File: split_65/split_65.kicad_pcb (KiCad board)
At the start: 2 copper layers, 156 parts, among them SW1 SW_Push, SW10 SW_Push, SW11 SW_Push, SW12 SW_Push, SW13 SW_Push, SW14 SW_Push, SW15 SW_Push, SW16 SW_Push, SW17 SW_Push, SW18 SW_Push, SW19 SW_Push, SW2 SW_Push, SW20 SW_Push, SW21 SW_Push, SW22 SW_Push, SW23 SW_Push, SW24 SW_Push, SW25 SW_Push, SW26 SW_Push, SW27 SW_Push, SW28 SW_Push, SW29 SW_Push, SW3 SW_Push, SW30 SW_Push, SW31 SW_Push, SW32 SW_Push, SW33 SW_Push, SW34 SW_Push, SW35 SW_Push, SW36 SW_Push, SW37 SW_Push, SW38 SW_Push, SW39 SW_Push, SW4 SW_Push, SW40 SW_Push, SW41 SW_Push, SW42 SW_Push, SW43 SW_Push, SW44 SW_Push, SW45 SW_Push, SW46 SW_Push, SW47 SW_Push, SW48 SW_Push, SW49 SW_Push, SW5 SW_Push, SW50 SW_Push, SW51 SW_Push, SW52 SW_Push, SW53 SW_Push, SW54 SW_Push, SW55 SW_Push, SW56 SW_Push, SW57 SW_Push, SW58 SW_Push, SW59 SW_Push, SW6 SW_Push, SW60 SW_Push, SW61 SW_Push, SW62 SW_Push, SW63 SW_Push, SW64 SW_Push, SW65 SW_Push, SW66 SW_Push, SW67 SW_Push, SW68 SW_Push, SW69 SW_Push, SW7 SW_Push, SW70 SW_Push, SW71 SW_Push, SW72 SW_Push, SW73 SW_Push, SW74 SW_Push, SW75 SW_Push, SW76 SW_Push, SW77 SW_Push, SW78 SW_Push, SW79 SW_Push, SW8 SW_Push, SW80 SW_Push, SW81 SW_Push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

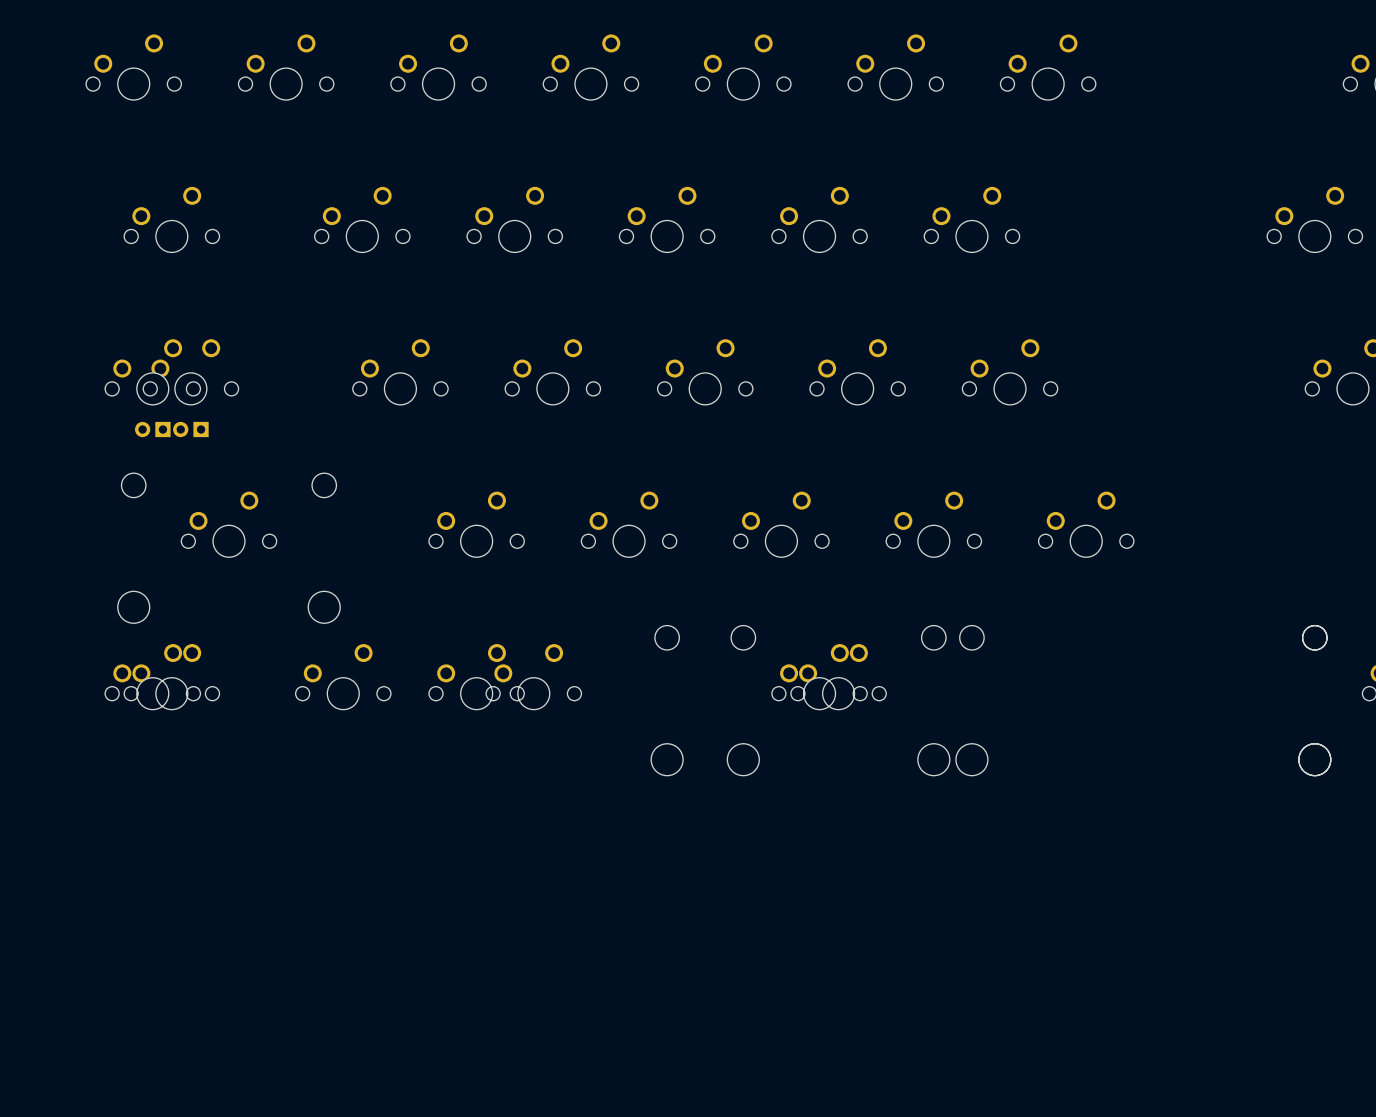
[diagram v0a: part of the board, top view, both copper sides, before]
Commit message: setup schematic hierarchies, update images
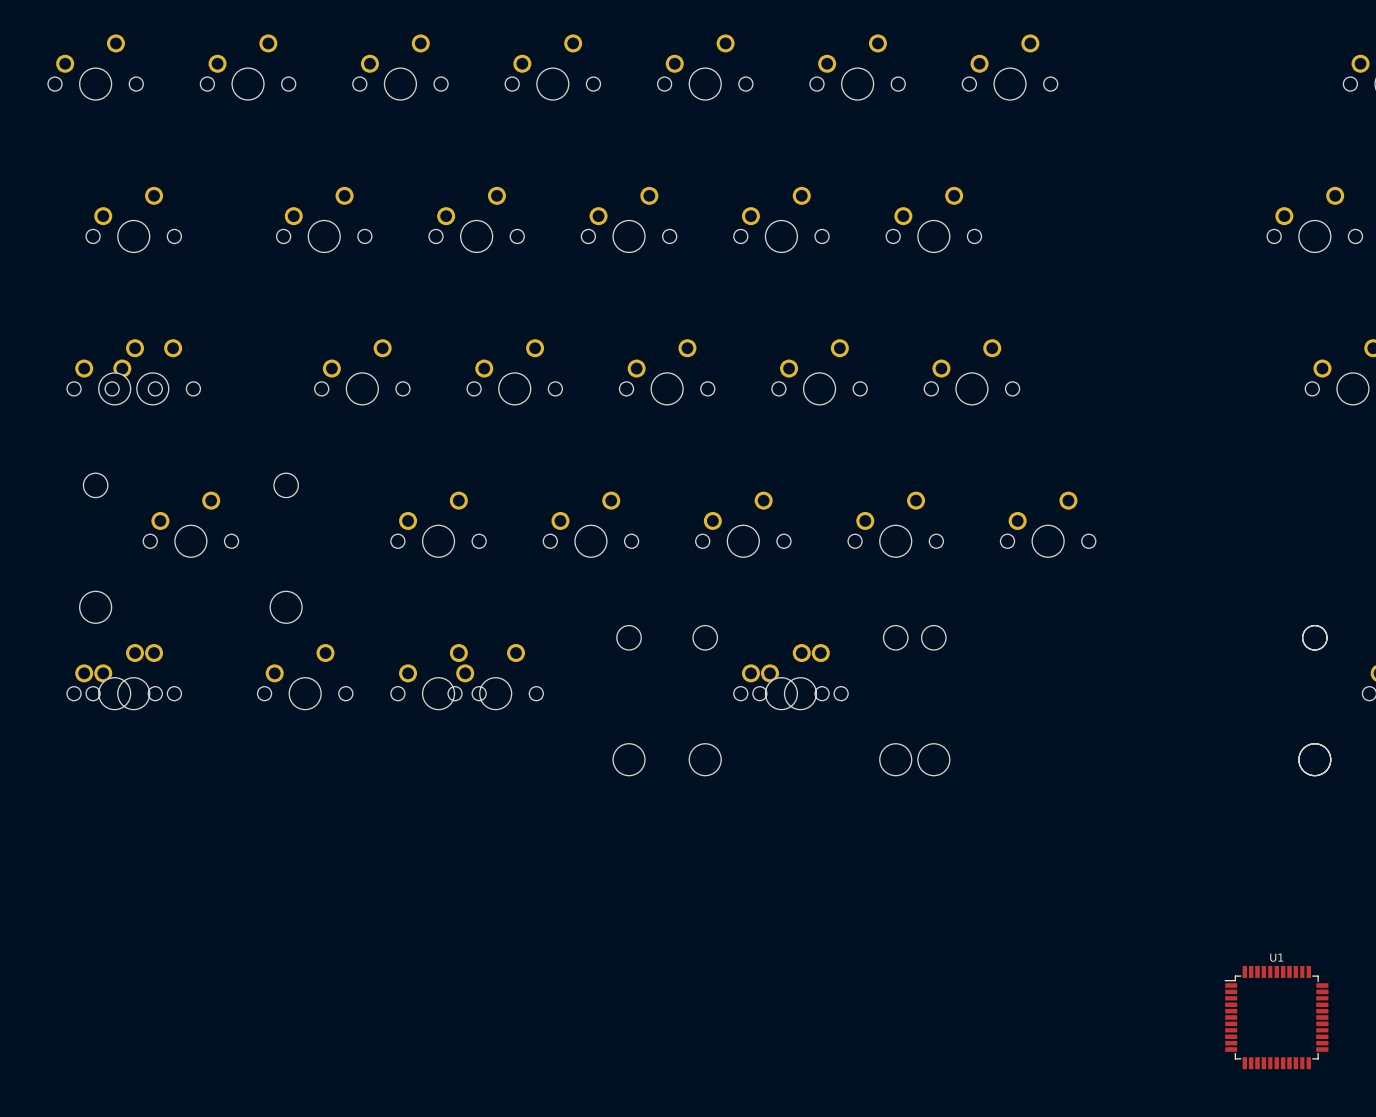
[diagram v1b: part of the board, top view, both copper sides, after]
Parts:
- added U1: ATmega32U4-AU, Package_QFP:TQFP-44_10x10mm_P0.8mm, F.Cu at (211.9, 154.8)
- SW10: footprint MX_Alps_Hybrid:MXOnly-1.25U-NoLED -> MX_Alps_Hybrid:MXOnly-2.25U-NoLED
- SW11, SW17: footprint MX_Alps_Hybrid:MXOnly-1.5U-NoLED -> MX_Alps_Hybrid:MXOnly-1.25U-NoLED
- SW12, SW18: footprint MX_Alps_Hybrid:MXOnly-1U-NoLED -> MX_Alps_Hybrid:MXOnly-1.5U-NoLED
- SW16, SW22: footprint MX_Alps_Hybrid:MXOnly-1.25U-NoLED -> MX_Alps_Hybrid:MXOnly-1U-NoLED
- SW23: footprint MX_Alps_Hybrid:MXOnly-1U-NoLED -> MX_Alps_Hybrid:MXOnly-1.25U-NoLED
- SW27: footprint MX_Alps_Hybrid:MXOnly-2.75U-NoLED -> MX_Alps_Hybrid:MXOnly-1U-NoLED
- SW28: footprint MX_Alps_Hybrid:MXOnly-3U-NoLED -> MX_Alps_Hybrid:MXOnly-2.75U-NoLED
- SW29: footprint MX_Alps_Hybrid:MXOnly-1U-NoLED -> MX_Alps_Hybrid:MXOnly-3U-NoLED
- SW6: footprint MX_Alps_Hybrid:MXOnly-1.5U-NoLED -> MX_Alps_Hybrid:MXOnly-1U-NoLED
- SW7: footprint MX_Alps_Hybrid:MXOnly-1.75U -> MX_Alps_Hybrid:MXOnly-1.5U-NoLED
- SW8: footprint MX_Alps_Hybrid:MXOnly-1.25U -> MX_Alps_Hybrid:MXOnly-1.75U-NoLED
- SW9: footprint MX_Alps_Hybrid:MXOnly-2.25U-NoLED -> MX_Alps_Hybrid:MXOnly-1.25U-NoLED
- moved SW5 81.4 mm to (40.5, 114.3)
- moved SW12 78.5 mm to (69.1, 114.3)
- moved SW23 77.1 mm to (114.3, 114.3)
- moved SW29 76.3 mm to (150.0, 114.3)
- moved SW18 76.2 mm to (107.2, 114.3)
- moved SW33 57.1 mm to (164.3, 95.2)
- moved SW37 57.1 mm to (183.4, 95.2)
- moved SW1 30.5 mm to (64.3, 38.1)
- moved SW26 23.8 mm to (135.7, 76.2)
- moved SW15 23.8 mm to (97.6, 76.2)
- moved SW9 23.8 mm to (66.7, 76.2)
- moved SW21 23.8 mm to (116.7, 76.2)
- moved SW32 23.8 mm to (154.8, 76.2)
- moved SW36 23.8 mm to (173.8, 76.2)
- moved SW16 22.5 mm to (107.2, 95.2)
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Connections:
- D29 pad 1: Net-(D10-Pad1) -> Net-(D14-Pad1)
- D33 pad 1: Net-(D10-Pad1) -> Net-(D14-Pad1)
- SW11 pad 1: Net-(D9-Pad2) -> Net-(D10-Pad2)
- SW12 pad 2: Net-(SW12-Pad2) -> Net-(SW10-Pad2)
- SW13 pad 2: Net-(SW12-Pad2) -> Net-(SW13-Pad2)
- SW14 pad 2: Net-(SW12-Pad2) -> Net-(SW13-Pad2)
- SW15 pad 2: Net-(SW12-Pad2) -> Net-(SW13-Pad2)
- SW16 pad 2: Net-(SW12-Pad2) -> Net-(SW13-Pad2)
- SW17 pad 1: Net-(D14-Pad2) -> Net-(D15-Pad2)
- SW17 pad 2: Net-(SW12-Pad2) -> Net-(SW13-Pad2)
- SW18 pad 2: Net-(SW18-Pad2) -> Net-(SW13-Pad2)
- SW19 pad 2: Net-(SW18-Pad2) -> Net-(SW19-Pad2)
- SW20 pad 2: Net-(SW18-Pad2) -> Net-(SW19-Pad2)
- SW21 pad 2: Net-(SW18-Pad2) -> Net-(SW19-Pad2)
- SW22 pad 2: Net-(SW18-Pad2) -> Net-(SW19-Pad2)
- SW23 pad 2: Net-(SW23-Pad2) -> Net-(SW19-Pad2)
- SW24 pad 2: Net-(SW23-Pad2) -> Net-(SW24-Pad2)
- SW25 pad 2: Net-(SW23-Pad2) -> Net-(SW24-Pad2)
- SW26 pad 2: Net-(SW23-Pad2) -> Net-(SW24-Pad2)
- SW27 pad 2: Net-(SW23-Pad2) -> Net-(SW24-Pad2)
- SW28 pad 1: Net-(D24-Pad2) -> Net-(D25-Pad2)
- SW28 pad 2: Net-(SW23-Pad2) -> Net-(SW24-Pad2)
- SW29 pad 2: Net-(SW29-Pad2) -> Net-(SW24-Pad2)
- SW30 pad 2: Net-(SW29-Pad2) -> Net-(SW30-Pad2)
- SW31 pad 2: Net-(SW29-Pad2) -> Net-(SW30-Pad2)
- SW32 pad 2: Net-(SW29-Pad2) -> Net-(SW30-Pad2)
- SW33 pad 2: Net-(SW33-Pad2) -> Net-(SW30-Pad2)
- SW34 pad 2: Net-(SW33-Pad2) -> Net-(SW34-Pad2)
- SW35 pad 2: Net-(SW33-Pad2) -> Net-(SW34-Pad2)
- SW36 pad 2: Net-(SW33-Pad2) -> Net-(SW34-Pad2)
- SW37 pad 2: Net-(SW37-Pad2) -> Net-(SW34-Pad2)
- SW5 pad 2: Net-(SW10-Pad2) -> Net-(SW1-Pad2)
- SW8 pad 1: Net-(D7-Pad2) -> Net-(D8-Pad2)
